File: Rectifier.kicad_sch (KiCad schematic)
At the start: 8 parts

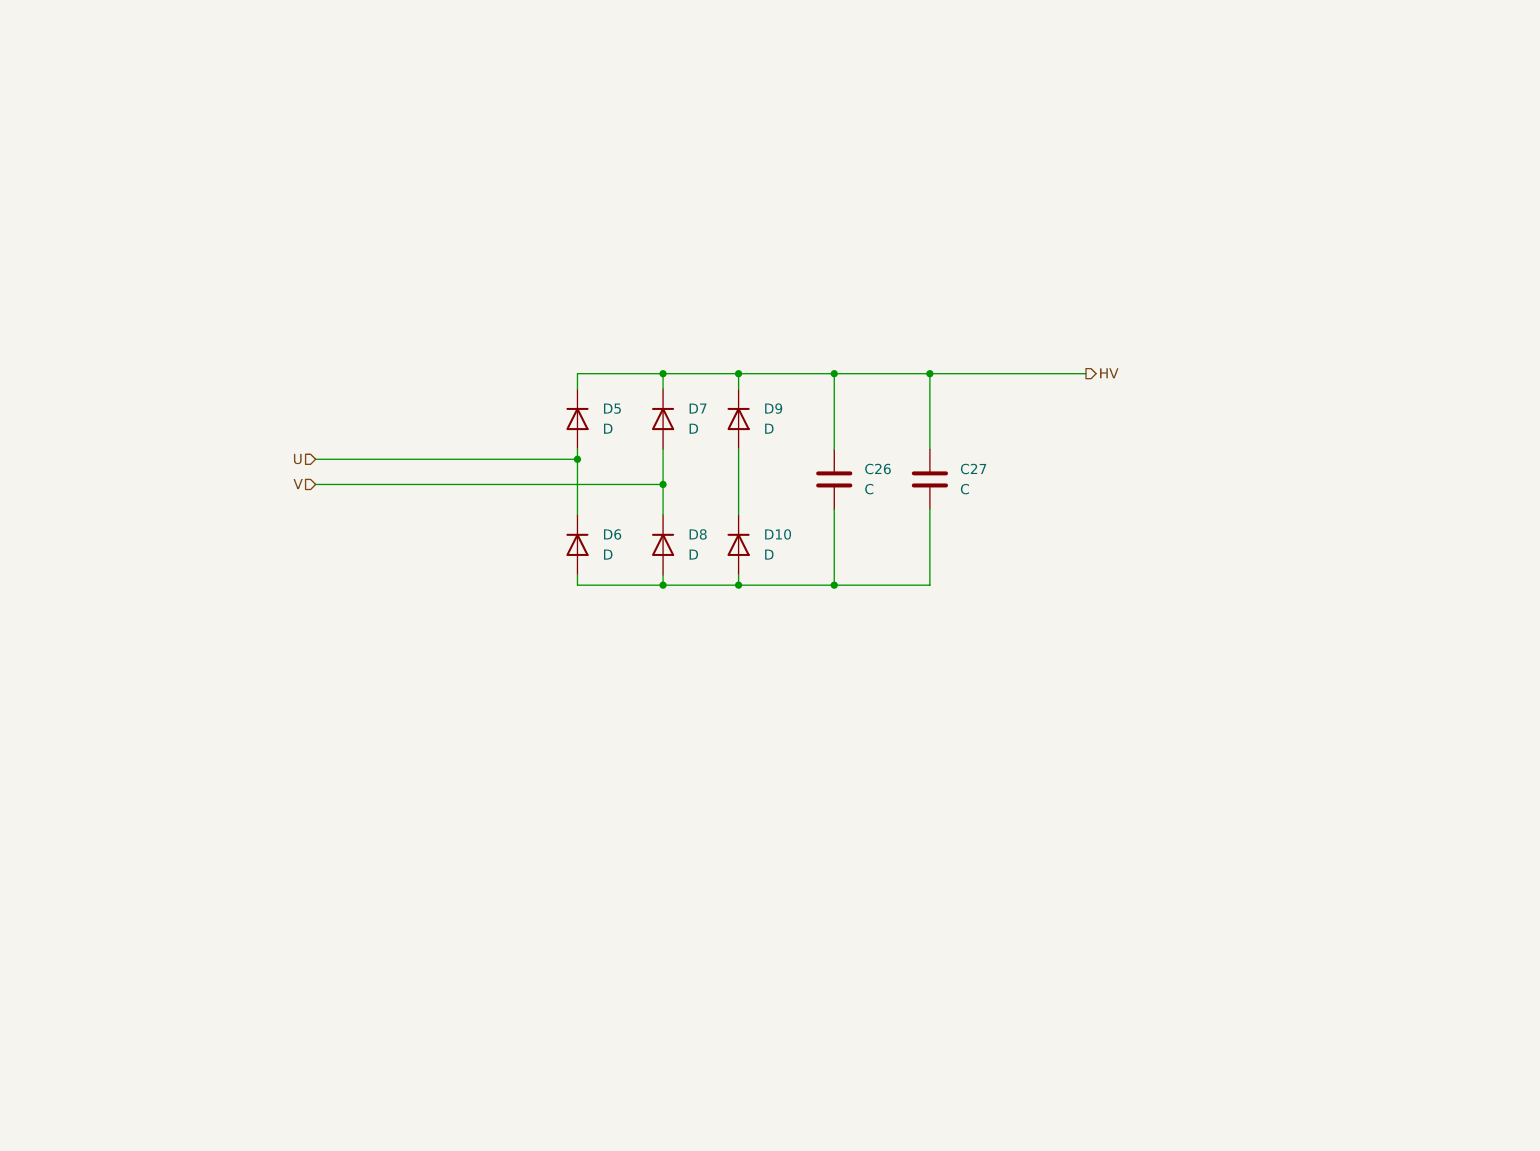
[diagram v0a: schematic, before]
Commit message: update power supply page
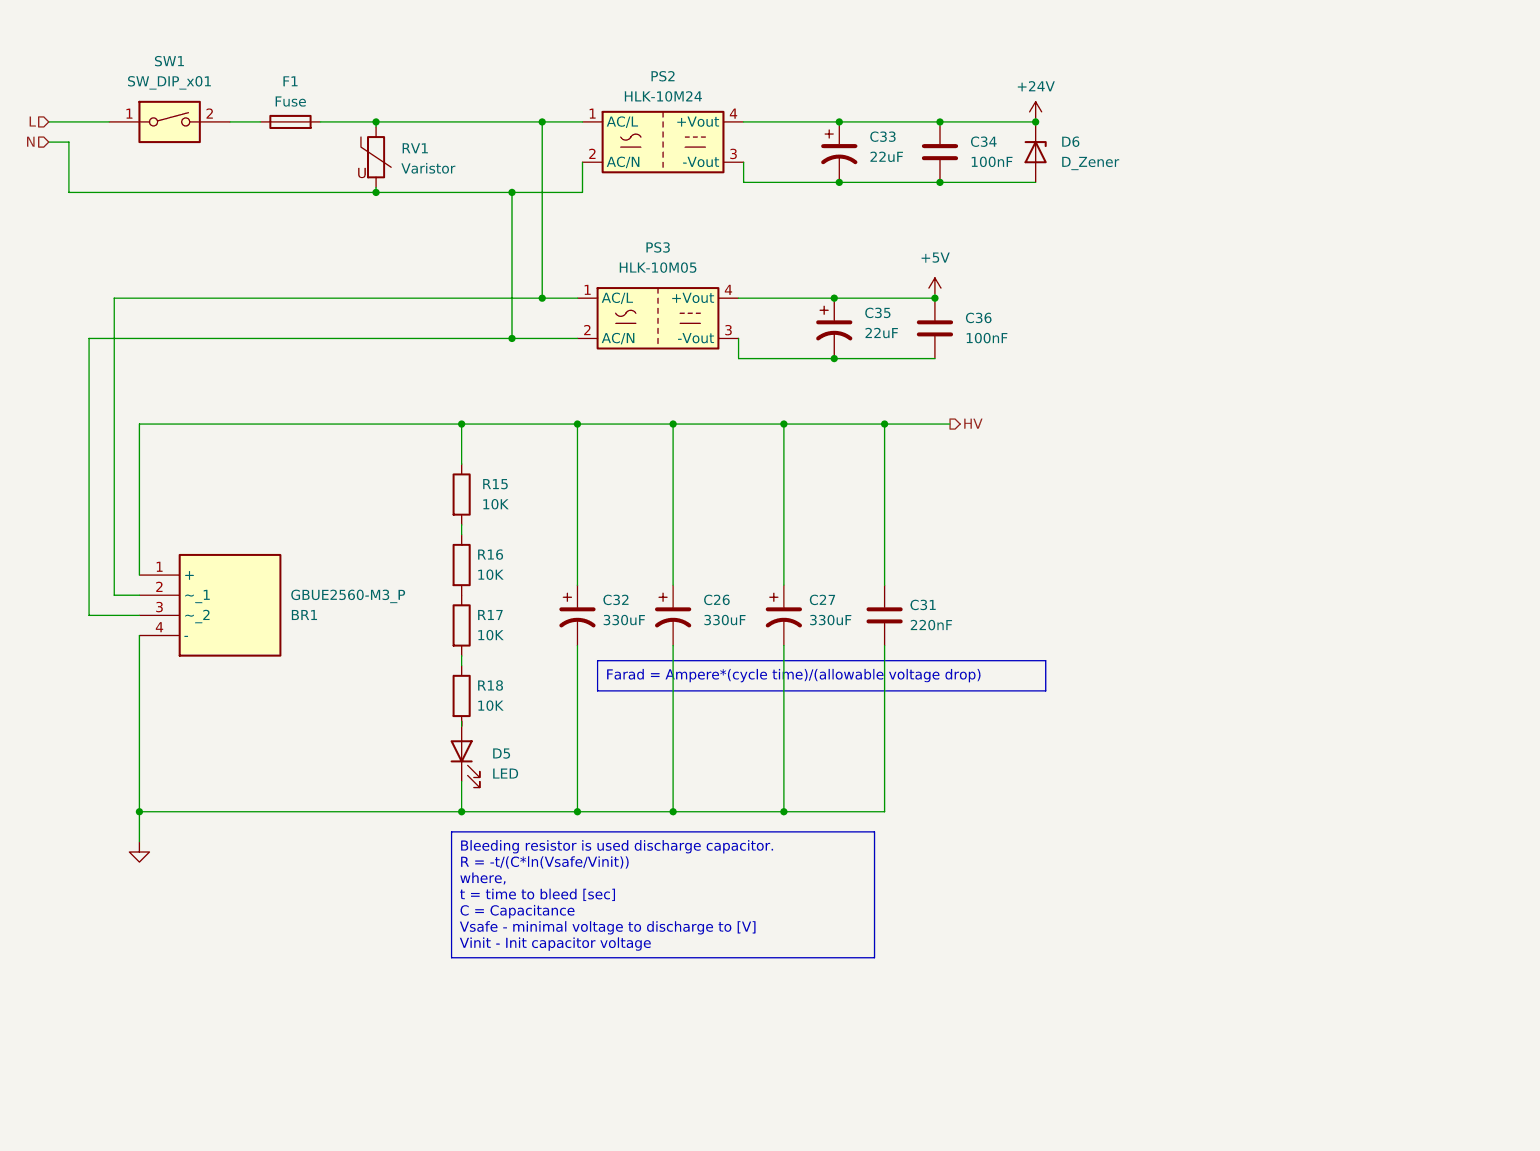
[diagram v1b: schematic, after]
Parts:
- removed C26, C27: C, symbol Device:C
- removed D10, D5, D6, D7, D8, D9: D, symbol Device:D
- added BR1: GBUE2560-M3_P, GBUE2560M3P, symbol SamacSys_Parts:GBUE2560-M3_P
- added C26, C27, C32: 330uF, symbol Device:C_Polarized_US
- added C31: 220nF, symbol Device:C
- added C33, C35: 22uF, symbol Device:C_Polarized_US
- added C34, C36: 100nF, symbol Device:C
- added D5: LED, symbol Device:LED
- added D6: D_Zener, symbol Device:D_Zener
- added F1: Fuse, symbol Device:Fuse
- added PS2: HLK-10M24, Converter_ACDC:Converter_ACDC_HiLink_HLK-10Mxx, symbol Converter_ACDC:HLK-10M24
- added PS3: HLK-10M05, Converter_ACDC:Converter_ACDC_HiLink_HLK-10Mxx, symbol Converter_ACDC:HLK-10M05
- added R15, R16, R17, R18: 10K, symbol Device:R
- added RV1: Varistor, symbol Device:Varistor
- added SW1: SW_DIP_x01, symbol Switch:SW_DIP_x01
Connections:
- net HV: now also BR1.1 (+), C26.1, C27.1, C31.1, C32.1, R15.1
- new net: BR1.2 (~_1), F1.2, PS2.1 (AC/L), PS3.1 (AC/L), RV1.1
- new net: C35.2, C36.2, PS3.3 (-Vout)
- new net: R15.2, R16.1
- new net: R17.2, R18.1
- new net: D5.2 (A), R18.2
- new net: F1.1, SW1.2
- new net: C33.2, C34.2, D6.2 (A), PS2.3 (-Vout)
- new net: R16.2, R17.1
- new net +24V: C33.1, C34.1, D6.1 (K), PS2.4 (+Vout)
- new net +5V: C35.1, C36.1, PS3.4 (+Vout)
- new net GND: BR1.4 (-), C26.2, C27.2, C31.2, C32.2, D5.1 (K)
- new net L: SW1.1
- new net N: BR1.3 (~_2), PS2.2 (AC/N), PS3.2 (AC/N), RV1.2

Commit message: update power label
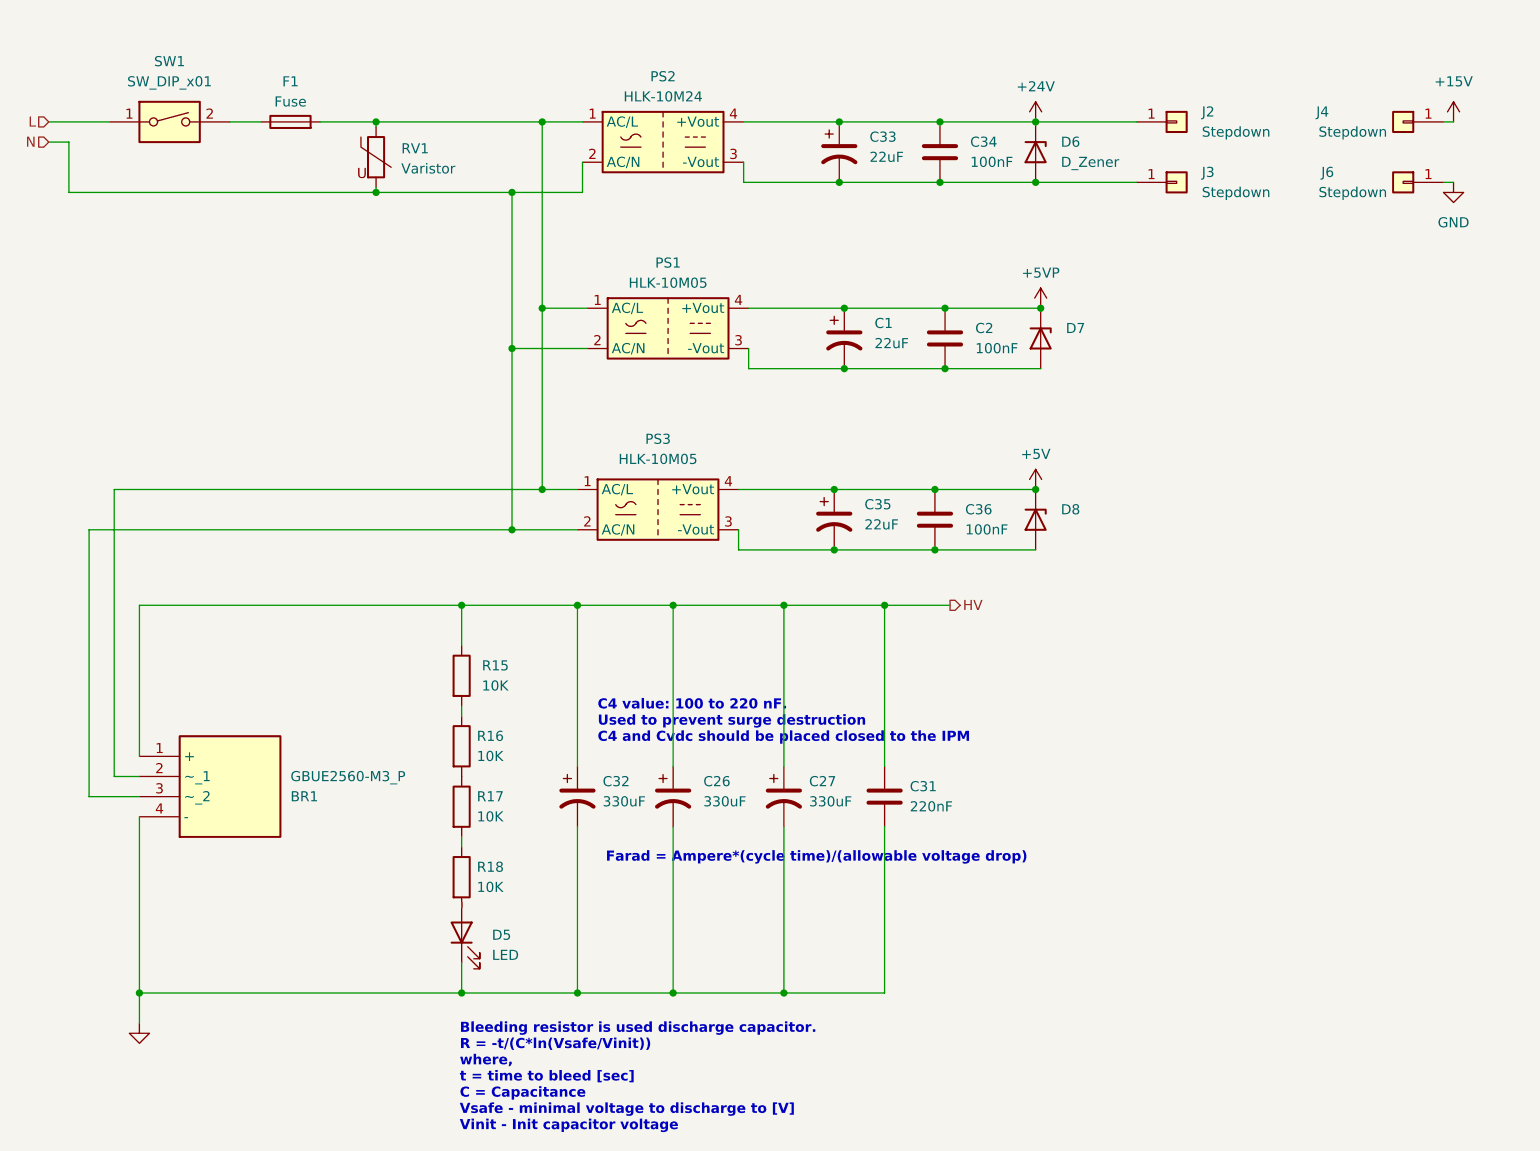
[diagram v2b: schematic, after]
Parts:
- added C1: 22uF, symbol Device:C_Polarized_US
- added C2: 100nF, symbol Device:C
- added D7, D8: D_Zener, symbol Device:D_Zener
- added J2, J3, J4, J6: Stepdown, symbol Connector_Generic:Conn_01x01
- added PS1: HLK-10M05, Converter_ACDC:Converter_ACDC_HiLink_HLK-10Mxx, symbol Converter_ACDC:HLK-10M05
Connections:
- net +24V: now also J2.1 (Pin_1)
- net +5V: now also D8.1 (K)
- net GND: now also J6.1 (Pin_1)
- net N: now also PS1.2 (AC/N)
- net at BR1.2 (~_1), F1.2, PS2.1 (AC/L)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: now also PS1.1 (AC/L)
- net at C35.2, C36.2, PS3.3 (-Vout): now also D8.2 (A)
- net at C33.2, C34.2, D6.2 (A)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: now also J3.1 (Pin_1)
- new net: C1.2, C2.2, D7.2 (A), PS1.3 (-Vout)
- new net +15V: J4.1 (Pin_1)
- new net +5VP: C1.1, C2.1, D7.1 (K), PS1.4 (+Vout)
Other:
- note added: "C4 value: 100 to 220 nF. Used to prevent surge destruction C4 and Cvdc should be placed closed to the IPM"
- moved on the sheet: BR1, C26, C27, C31, C32, C35, C36, D5, PS3, R15, R16, R17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

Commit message: adding high speed isolator
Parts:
- BR1: footprint GBUE2560M3P -> SamacSys_Parts:GBUE2560M3P
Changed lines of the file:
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@@
       (effects (font (size 1.27 1.27)) (justify left))
     )
-    (property "Footprint" "GBUE2560M3P" (at 53.34 16.84 0)
+    (property "Footprint" "SamacSys_Parts:GBUE2560M3P" (at 53.34 16.84 0)
       (effects (font (size 1.27 1.27)) (justify left top) hide)
     )

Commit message: updating component & board
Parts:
- removed C26, C27: 330uF, symbol Device:C_Polarized_US
- C32: value 330uF -> 330uF 400V
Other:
- moved on the sheet: C31
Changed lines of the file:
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@@
   (junction (at 74.93 85.09) (diameter 0) (color 0 0 0 0)
   )
-  (junction (at 115.57 133.985) (diameter 0) (color 0 0 0 0)
-  )
   (junction (at 121.92 70.485) (diameter 0) (color 0 0 0 0)
   )
@@
   (junction (at 147.32 24.13) (diameter 0) (color 0 0 0 0)
   )
-  (junction (at 128.27 85.09) (diameter 0) (color 0 0 0 0)
+  (junction (at 103.505 85.09) (diameter 0) (color 0 0 0 0)
   )
   (junction (at 121.92 78.105) (diameter 0) (color 0 0 0 0)
@@
   (junction (at 85.09 70.485) (diameter 0) (color 0 0 0 0)
   )
-  (junction (at 101.6 85.09) (diameter 0) (color 0 0 0 0)
-  )
   (junction (at 123.19 47.625) (diameter 0) (color 0 0 0 0)
   )
@@
   (junction (at 147.955 47.625) (diameter 0) (color 0 0 0 0)
   )
-  (junction (at 115.57 85.09) (diameter 0) (color 0 0 0 0)
-  )
   (junction (at 89.535 85.09) (diameter 0) (color 0 0 0 0)
   )
-  (junction (at 101.6 133.985) (diameter 0) (color 0 0 0 0)
-  )
   (junction (at 134.62 78.105) (diameter 0) (color 0 0 0 0)
   )
@@
   (junction (at 135.255 31.75) (diameter 0) (color 0 0 0 0)
   )
-  (wire (pts (xy 115.57 85.09) (xy 115.57 105.41))
-    (stroke (width 0) (type default))
-  )
   (wire (pts (xy 81.28 52.705) (xy 81.28 75.565))
     (stroke (width 0) (type default))
   )
-  (wire (pts (xy 101.6 85.09) (xy 101.6 105.41))
-    (stroke (width 0) (type default))
-  )
   (wire (pts (xy 74.93 114.3) (xy 74.93 115.57))
     (stroke (width 0) (type default))
@@
     (stroke (width 0) (type default))
   )
+  (wire (pts (xy 74.93 85.09) (xy 89.535 85.09))
+    (stroke (width 0) (type default))
+  )
   (wire (pts (xy 89.535 85.09) (xy 89.535 105.41))
     (stroke (width 0) (type default))
   )
-  (wire (pts (xy 115.57 85.09) (xy 128.27 85.09))
-    (stroke (width 0) (type default))
-  )
   (wire (pts (xy 34.29 85.09) (xy 74.93 85.09))
     (stroke (width 0) (type default))
@@
     (stroke (width 0) (type default))
   )
-  (wire (pts (xy 74.93 85.09) (xy 89.535 85.09))
-    (stroke (width 0) (type default))
-  )
   (wire (pts (xy 34.29 85.09) (xy 34.29 104.14))
     (stroke (width 0) (type default))
   )
-  (wire (pts (xy 101.6 133.985) (xy 115.57 133.985))
-    (stroke (width 0) (type default))
-  )
   (wire (pts (xy 25.4 26.67) (xy 25.4 33.02))
     (stroke (width 0) (type default))
   )
-  (wire (pts (xy 128.27 85.09) (xy 136.525 85.09))
+  (wire (pts (xy 103.505 85.09) (xy 111.76 85.09))
     (stroke (width 0) (type default))
   )
@@
     (stroke (width 0) (type default))
   )
+  (wire (pts (xy 89.535 133.985) (xy 103.505 133.985))
+    (stroke (width 0) (type default))
+  )
   (wire (pts (xy 74.93 130.175) (xy 74.93 133.985))
     (stroke (width 0) (type default))
@@
     (stroke (width 0) (type default))
   )
-  (wire (pts (xy 115.57 113.03) (xy 115.57 133.985))
-    (stroke (width 0) (type default))
-  )
   (wire (pts (xy 74.93 85.09) (xy 74.93 90.17))
     (stroke (width 0) (type default))
@@
     (stroke (width 0) (type default))
   )
-  (wire (pts (xy 89.535 133.985) (xy 101.6 133.985))
+  (wire (pts (xy 74.93 133.985) (xy 89.535 133.985))
     (stroke (width 0) (type default))
   )
@@
     (stroke (width 0) (type default))
   )
-  (wire (pts (xy 128.27 113.03) (xy 128.27 133.985))
+  (wire (pts (xy 103.505 113.03) (xy 103.505 133.985))
     (stroke (width 0) (type default))
   )
@@
     (stroke (width 0) (type default))
   )
-  (wire (pts (xy 101.6 85.09) (xy 115.57 85.09))
-    (stroke (width 0) (type default))
-  )
-  (wire (pts (xy 115.57 133.985) (xy 128.27 133.985))
+  (wire (pts (xy 89.535 85.09) (xy 103.505 85.09))
     (stroke (width 0) (type default))
   )
@@
     (stroke (width 0) (type default))
   )
-  (wire (pts (xy 74.93 133.985) (xy 89.535 133.985))
-    (stroke (width 0) (type default))
-  )
   (wire (pts (xy 81.28 33.02) (xy 90.17 33.02))
     (stroke (width 0) (type default))
@@
     (stroke (width 0) (type default))
   )
-  (wire (pts (xy 128.27 85.09) (xy 128.27 105.41))
+  (wire (pts (xy 103.505 85.09) (xy 103.505 105.41))
     (stroke (width 0) (type default))
   )
@@
     (stroke (width 0) (type default))
   )
-  (wire (pts (xy 101.6 113.03) (xy 101.6 133.985))
-    (stroke (width 0) (type default))
-  )
   (wire (pts (xy 111.125 47.625) (xy 123.19 47.625))
     (stroke (width 0) (type default))
   )
   (wire (pts (xy 85.09 24.13) (xy 90.17 24.13))
-    (stroke (width 0) (type default))
-  )
-  (wire (pts (xy 89.535 85.09) (xy 101.6 85.09))
     (stroke (width 0) (type default))
   )
@@
   )
   (text_box "Farad = Ampere*(cycle time)/(allowable voltage drop)"
-    (at 92.075 114.935 0) (size 56.515 3.81)
+    (at 142.24 99.06 0) (size 56.515 3.81)
     (stroke (width -0.0001) (type default))
     (fill (type none))
@@
   )
   (text "C4 value: 100 to 220 nF.\nUsed to prevent surge destruction\nC4 and Cvdc should be placed closed to the IPM\n\n\n"
-    (at 92.075 106.68 0)
+    (at 143.51 114.3 0)
     (effects (font (size 1.27 1.27) bold) (justify left bottom))
   )
@@
     (effects (font (size 1.27 1.27)) (justify right))
   )
-  (hierarchical_label "HV" (shape output) (at 136.525 85.09 0) (fields_autoplaced)
+  (hierarchical_label "HV" (shape output) (at 111.76 85.09 0) (fields_autoplaced)
     (effects (font (size 1.27 1.27)) (justify left))
   )
@@
     )
   )
-  (symbol (lib_id "Device:C_Polarized_US") (at 101.6 109.22 0) (unit 1)
-    (in_bom yes) (on_board yes) (dnp no) (fields_autoplaced)
-    (property "Reference" "C26" (at 105.41 107.315 0)
-      (effects (font (size 1.27 1.27)) (justify left))
-    )
-    (property "Value" "330uF" (at 105.41 109.855 0)
-      (effects (font (size 1.27 1.27)) (justify left))
-    )
-    (property "Footprint" "" (at 101.6 109.22 0)
-      (effects (font (size 1.27 1.27)) hide)
-    )
-    (property "Datasheet" "~" (at 101.6 109.22 0)
-      (effects (font (size 1.27 1.27)) hide)
-    )
-    (pin "1")
-    (pin "2")
-    (instances
-      (project "Main"
-        (path "/c97a22ab-71f8-4b91-b313-15b8a3e640d7/411c259b-3fdf-42a4-b1dc-bccd2acfc8e5"
-          (reference "C26") (unit 1)
-        )
-      )
-    )
-  )
   (symbol (lib_id "Device:D_Zener") (at 147.955 51.435 270) (unit 1)
     (in_bom yes) (on_board yes) (dnp no) (fields_autoplaced)
@@
         (path "/c97a22ab-71f8-4b91-b313-15b8a3e640d7/411c259b-3fdf-42a4-b1dc-bccd2acfc8e5"
           (reference "PS2") (unit 1)
-        )
-      )
-    )
-  )
-  (symbol (lib_id "Device:C_Polarized_US") (at 115.57 109.22 0) (unit 1)
-    (in_bom yes) (on_board yes) (dnp no) (fields_autoplaced)
-    (property "Reference" "C27" (at 118.745 107.315 0)
-      (effects (font (size 1.27 1.27)) (justify left))
-    )
-    (property "Value" "330uF" (at 118.745 109.855 0)
-      (effects (font (size 1.27 1.27)) (justify left))
-    )
-    (property "Footprint" "" (at 115.57 109.22 0)
-      (effects (font (size 1.27 1.27)) hide)
-    )
-    (property "Datasheet" "~" (at 115.57 109.22 0)
-      (effects (font (size 1.27 1.27)) hide)
-    )
-    (pin "1")
-    (pin "2")
-    (instances
-      (project "Main"
-        (path "/c97a22ab-71f8-4b91-b313-15b8a3e640d7/411c259b-3fdf-42a4-b1dc-bccd2acfc8e5"
-          (reference "C27") (unit 1)
         )
       )
@@
   )
   (symbol (lib_id "Device:C_Polarized_US") (at 89.535 109.22 0) (unit 1)
-    (in_bom yes) (on_board yes) (dnp no) (fields_autoplaced)
-    (property "Reference" "C32" (at 92.71 107.315 0)
-      (effects (font (size 1.27 1.27)) (justify left))
-    )
-    (property "Value" "330uF" (at 92.71 109.855 0)
+    (in_bom yes) (on_board yes) (dnp no)
+    (property "Reference" "C32" (at 86.995 112.395 0)
+      (effects (font (size 1.27 1.27)) (justify left))
+    )
+    (property "Value" "330uF 400V" (at 86.995 114.935 0)
       (effects (font (size 1.27 1.27)) (justify left))
     )
@@
     )
   )
-  (symbol (lib_id "Device:C") (at 128.27 109.22 0) (unit 1)
-    (in_bom yes) (on_board yes) (dnp no) (fields_autoplaced)
-    (property "Reference" "C31" (at 131.445 107.95 0)
-      (effects (font (size 1.27 1.27)) (justify left))
-    )
-    (property "Value" "220nF" (at 131.445 110.49 0)
-      (effects (font (size 1.27 1.27)) (justify left))
-    )
-    (property "Footprint" "" (at 129.2352 113.03 0)
-      (effects (font (size 1.27 1.27)) hide)
-    )
-    (property "Datasheet" "~" (at 128.27 109.22 0)
-      (effects (font (size 1.27 1.27)) hide)
-    )
+  (symbol (lib_id "Device:C") (at 103.505 109.22 0) (unit 1)
+    (in_bom yes) (on_board yes) (dnp no) (fields_autoplaced)
+    (property "Reference" "C31" (at 106.68 107.95 0)
+      (effects (font (size 1.27 1.27)) (justify left))
+    )
+    (property "Value" "220nF" (at 106.68 110.49 0)
+      (effects (font (size 1.27 1.27)) (justify left))
+    )
+    (property "Footprint" "" (at 104.4702 113.03 0)
+      (effects (font (size 1.27 1.27)) hide)
+    )
+    (property "Datasheet" "~" (at 103.505 109.22 0)
+      (effects (font (size 1.27 1.27)) hide)
+    )
